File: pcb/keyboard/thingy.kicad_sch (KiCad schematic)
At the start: 49 parts, among them J1 Conn_02x09_Odd_Even, J10 Conn_01x04_Socket, J11 Conn_01x06_Pin, J12 Conn_01x06_Pin, J13 Conn_01x06_Pin, J14 Conn_01x04_Socket, J15 Conn_01x07_Socket, J16 Conn_01x04_MountingPin, J2 Conn_01x02_Socket, J3 Conn_01x02_Socket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

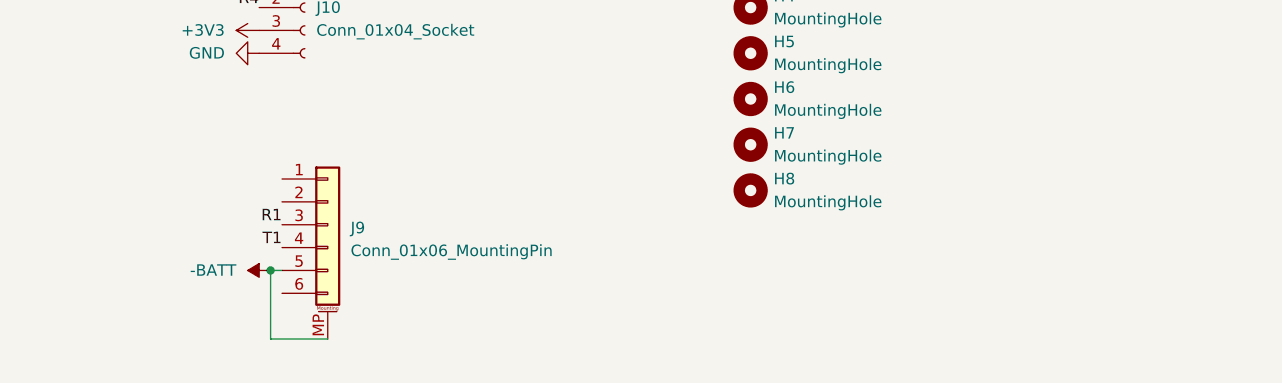
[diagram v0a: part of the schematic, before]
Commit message: placement verification
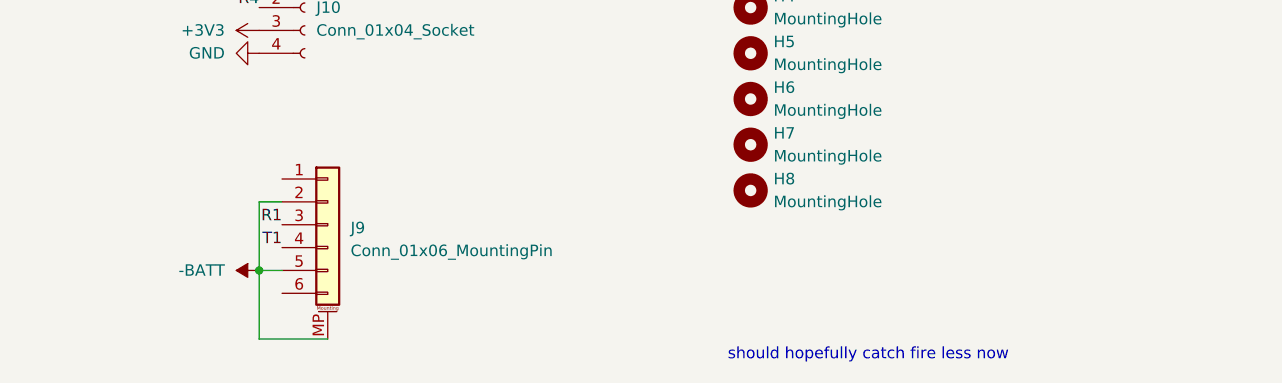
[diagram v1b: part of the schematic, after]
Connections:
- net -BATT: now also J9.2 (Pin_2)
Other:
- note added: "should hopefully catch fire less now"
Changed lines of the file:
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@@
   (junction (at 172.72 36.83) (diameter 0) (color 0 0 0 0)
   )
-  (junction (at 161.29 162.56) (diameter 0) (color 0 0 0 0)
-  )
   (junction (at 213.36 41.91) (diameter 0) (color 0 0 0 0)
   )
@@
   )
   (junction (at 59.69 156.21) (diameter 0) (color 0 0 0 0)
+  )
+  (junction (at 160.02 162.56) (diameter 0) (color 0 0 0 0)
   )
   (junction (at 149.86 36.83) (diameter 0) (color 0 0 0 0)
@@
     (stroke (width 0) (type default))
   )
+  (wire (pts (xy 160.02 162.56) (xy 160.02 154.94))
+    (stroke (width 0) (type default))
+  )
   (wire (pts (xy 52.07 156.21) (xy 59.69 156.21))
     (stroke (width 0) (type default))
@@
     (stroke (width 0) (type default))
   )
-  (wire (pts (xy 162.56 162.56) (xy 161.29 162.56))
-    (stroke (width 0) (type default))
-  )
   (wire (pts (xy 115.57 143.51) (xy 115.57 151.13))
     (stroke (width 0) (type default))
@@
     (stroke (width 0) (type default))
   )
+  (wire (pts (xy 160.02 162.56) (xy 162.56 162.56))
+    (stroke (width 0) (type default))
+  )
   (wire (pts (xy 39.37 147.32) (xy 39.37 148.59))
     (stroke (width 0) (type default))
@@
     (stroke (width 0) (type default))
   )
-  (wire (pts (xy 161.29 170.18) (xy 167.64 170.18))
+  (wire (pts (xy 160.02 154.94) (xy 162.56 154.94))
+    (stroke (width 0) (type default))
+  )
+  (wire (pts (xy 160.02 170.18) (xy 167.64 170.18))
     (stroke (width 0) (type default))
   )
@@
     (stroke (width 0) (type default))
   )
-  (wire (pts (xy 161.29 162.56) (xy 161.29 170.18))
+  (wire (pts (xy 160.02 162.56) (xy 160.02 170.18))
     (stroke (width 0) (type default))
   )
@@
   )
   (text "prev sensors\nQMC5883\nVL53L1X" (at 165.1 125.73 0)
+    (effects (font (size 1.27 1.27)) (justify left bottom))
+  )
+  (text "should hopefully catch fire less now" (at 212.09 172.72 0)
     (effects (font (size 1.27 1.27)) (justify left bottom))
   )
@@
     )
   )
-  (symbol (lib_id "power:-BATT") (at 161.29 162.56 90) (unit 1)
-    (in_bom yes) (on_board yes) (dnp no) (fields_autoplaced)
-    (property "Reference" "#PWR013" (at 165.1 162.56 0)
-      (effects (font (size 1.27 1.27)) hide)
-    )
-    (property "Value" "-BATT" (at 157.48 162.56 90)
-      (effects (font (size 1.27 1.27)) (justify left))
-    )
-    (property "Footprint" "" (at 161.29 162.56 0)
-      (effects (font (size 1.27 1.27)) hide)
-    )
-    (property "Datasheet" "" (at 161.29 162.56 0)
-      (effects (font (size 1.27 1.27)) hide)
-    )
+  (symbol (lib_id "power:-BATT") (at 160.02 162.56 90) (unit 1)
+    (in_bom yes) (on_board yes) (dnp no) (fields_autoplaced)
+    (property "Reference" "#PWR013" (at 163.83 162.56 0)
+      (effects (font (size 1.27 1.27)) hide)
+    )
+    (property "Value" "-BATT" (at 156.21 162.56 90)
+      (effects (font (size 1.27 1.27)) (justify left))
+    )
+    (property "Footprint" "" (at 160.02 162.56 0)
+      (effects (font (size 1.27 1.27)) hide)
+    )
+    (property "Datasheet" "" (at 160.02 162.56 0)
+      (effects (font (size 1.27 1.27)) hide)
+    )

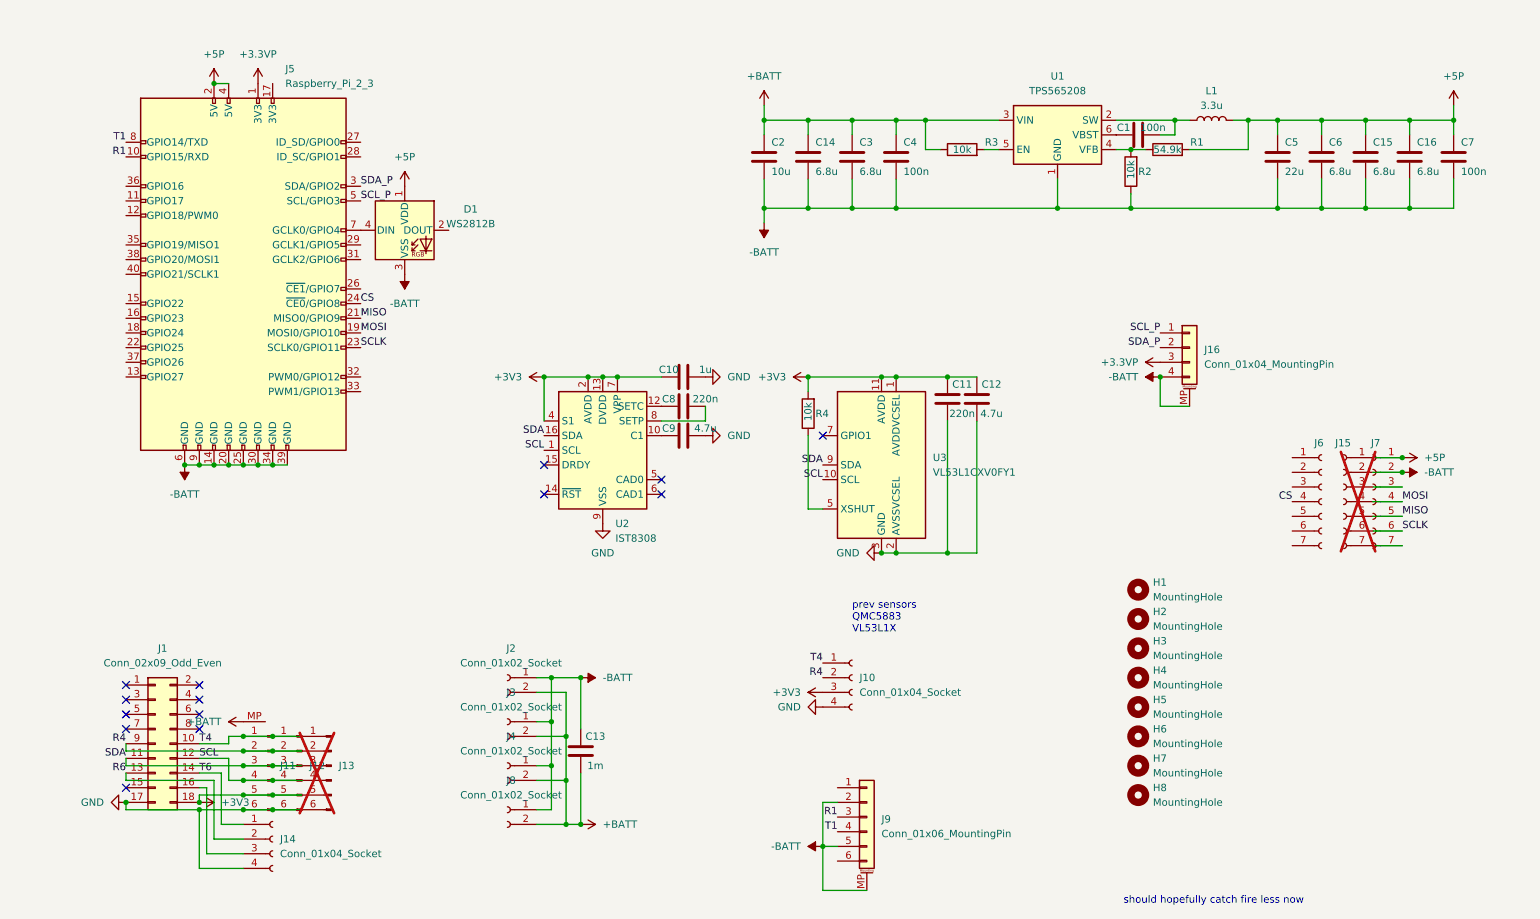
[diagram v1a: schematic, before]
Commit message: beginning schematic cleanup
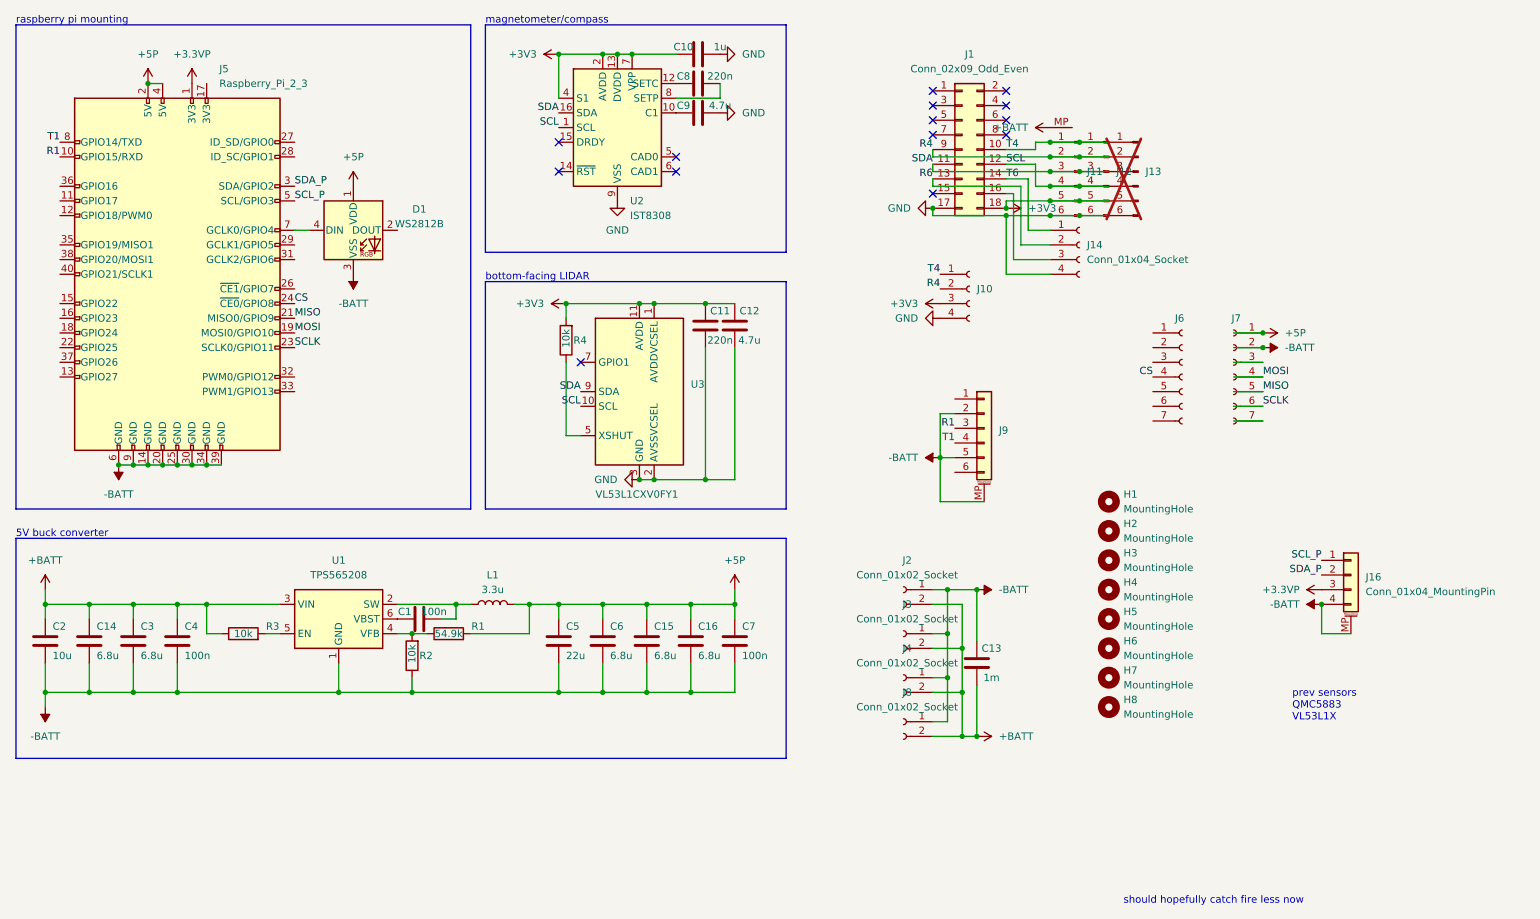
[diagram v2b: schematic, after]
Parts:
- removed J15: Conn_01x07_Socket, Connector_PinSocket_2.54mm:PinSocket_1x07_P2.54mm_Vertical_SMD_Pin1Left, symbol Connector:Conn_01x07_Socket
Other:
- note added: "5V buck converter"
- note added: "bottom-facing LIDAR"
- note added: "magnetometer/compass"
- note added: "raspberry pi mounting"
- moved on the sheet: C1, C10, C11, C12, C13, C14, C15, C16, C2, C3, C4, C5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

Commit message: tidy up keyboard
tidy up keyboard schematic and break out pi serial interfaces
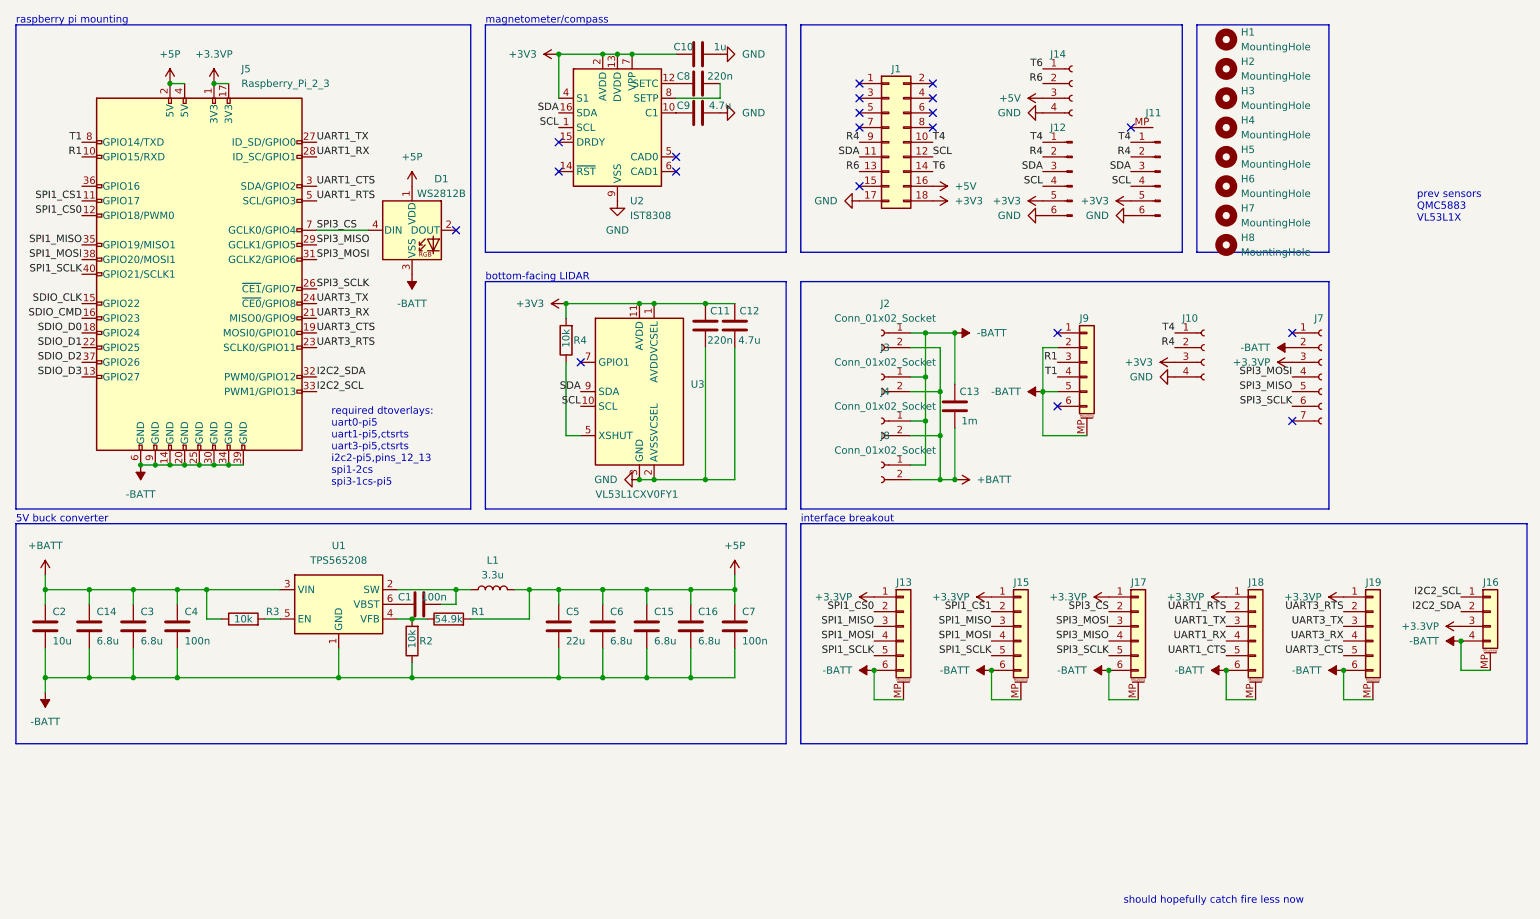
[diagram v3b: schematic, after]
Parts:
- removed J13: Conn_01x06_Pin, Connector_FFC-FPC:TE_84952-6_1x06-1MP_P1.0mm_Horizontal, symbol Connector:Conn_01x06_Pin
- removed J6: Conn_01x07_Socket, Connector_PinSocket_2.54mm:PinSocket_1x07_P2.54mm_Vertical, symbol Connector:Conn_01x07_Socket
- added J13, J15, J17, J18, J19: Conn_01x06, Connector_JST:JST_SH_BM06B-SRSS-TB_1x06-1MP_P1.00mm_Vertical, symbol Connector_Generic_MountingPin:Conn_01x06_MountingPin
- J10: footprint Connector_PinHeader_2.00mm:PinHeader_1x04_P2.00mm_Vertical -> Connector_PinHeader_2.54mm:PinHeader_1x04_P2.54mm_Vertical
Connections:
- net +3.3VP: now also J5.17 (3V3), J7.3 (Pin_3), J13.1 (Pin_1), J15.1 (Pin_1), J17.1 (Pin_1), J18.1 (Pin_1), J19.1 (Pin_1)
- net +5P: no longer J7.1 (Pin_1)
- net +BATT: no longer J11.MP (h)
- net -BATT: now also J13.6 (Pin_6), J13.MP (MountPin), J15.6 (Pin_6), J15.MP (MountPin), J17.6 (Pin_6), J17.MP (MountPin), J18.6 (Pin_6), J18.MP (MountPin), J19.6 (Pin_6), J19.MP (MountPin)
- net +5V: now reaches J1.16 (Pin_16), J14.3 (Pin_3)
- net SPI3_CS: now reaches D1.4 (DIN), J5.7 (GCLK0/GPIO4)
- net SPI3_CS: now also J17.2 (Pin_2)
- net SPI1_CS1: now reaches J5.11 (GPIO17)
- net SPI1_CS1: now also J15.2 (Pin_2)
- net SPI1_CS0: now reaches J5.12 (GPIO18/PWM0)
- net SPI1_CS0: now also J13.2 (Pin_2)
- net SDIO_D3: now reaches J5.13 (GPIO27)
- net SDIO_CLK: now reaches J5.15 (GPIO22)
- net SDIO_CMD: now reaches J5.16 (GPIO23)
- net SDIO_D0: now reaches J5.18 (GPIO24)
- net SDIO_D1: now reaches J5.22 (GPIO25)
- net SPI3_SCLK: now reaches J5.26 (~{CE1}/GPIO7)
- net SPI3_SCLK: now also J7.6 (Pin_6), J17.5 (Pin_5)
- net UART1_TX: now reaches J5.27 (ID_SD/GPIO0)
- net UART1_TX: now also J18.3 (Pin_3)
- net UART1_RX: now reaches J5.28 (ID_SC/GPIO1)
- net UART1_RX: now also J18.4 (Pin_4)
- net SPI3_MISO: now reaches J5.29 (GCLK1/GPIO5)
- net SPI3_MISO: now also J7.5 (Pin_5), J17.4 (Pin_4)
- net SPI3_MOSI: now reaches J5.31 (GCLK2/GPIO6)
- net SPI3_MOSI: now also J7.4 (Pin_4), J17.3 (Pin_3)
- net I2C2_SDA: now reaches J5.32 (PWM0/GPIO12)
- net I2C2_SDA: now also J16.2 (Pin_2)
- net I2C2_SCL: now reaches J5.33 (PWM1/GPIO13)
- net I2C2_SCL: now also J16.1 (Pin_1)
- net SPI1_MISO: now reaches J5.35 (GPIO19/MISO1)
- net SPI1_MISO: now also J13.3 (Pin_3), J15.3 (Pin_3)
- net SDIO_D2: now reaches J5.37 (GPIO26)
- net SPI1_MOSI: now reaches J5.38 (GPIO20/MOSI1)
- net SPI1_MOSI: now also J13.4 (Pin_4), J15.4 (Pin_4)
- net SPI1_SCLK: now reaches J5.40 (GPIO21/SCLK1)
- net SPI1_SCLK: now also J13.5 (Pin_5), J15.5 (Pin_5)
- net CS renamed UART3_TX
- net UART3_TX: now also J19.3 (Pin_3)
- net MISO renamed UART3_RX
- net UART3_RX: now also J19.4 (Pin_4); no longer J7.5 (Pin_5)
- net MOSI renamed UART3_CTS
- net UART3_CTS: now also J19.5 (Pin_5); no longer J7.4 (Pin_4)
- net SCLK renamed UART3_RTS
- net UART3_RTS: now also J19.2 (Pin_2); no longer J7.6 (Pin_6)
- net SCL_P renamed UART1_RTS
- net UART1_RTS: now also J18.2 (Pin_2); no longer J16.1 (Pin_1)
- net SDA_P renamed UART1_CTS
- net UART1_CTS: now also J18.5 (Pin_5); no longer J16.2 (Pin_2)
- no-connect marks 14 -> 20
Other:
- note added: "interface breakout"
- note added: "required dtoverlays: uart0-pi5 uart1-pi5,ctsrts uart3-pi5,ctsrts i2c2-pi5,pins_12_13 spi1-2cs spi3-1cs-pi5"
- moved on the sheet: C1, C13, C14, C15, C16, C2, C3, C4, C5, C6, C7, D1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
